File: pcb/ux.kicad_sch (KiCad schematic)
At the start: 41 parts, among them J5 Conn_01x40, J7 GameBoy_LinkPort, J8 Conn_01x02, SW12 A, SW13 B, SW14 START, SW15 SELECT, SW2 BOOT, SW3 RESET, SW4 UP, SW5 DOWN, SW6 LEFT, SW7 RIGHT, U5 APA2502, U7 ICM-42670-P, U8 TCA9535RTWR

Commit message: pcb: Update schematic to WIP6
Change-Id: I9e9f727ad2774ee986f2f97450dc509901129aec
Reviewed-on: https://pigweed-review.googlesource.com/c/pigweed/kudzu/+/169650
Reviewed-by: Anthony DiGirolamo <tonymd@google.com>
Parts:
- added C16 (x2): 10nF, symbol Device:C_Small
- added C17 (x2), C18: 100nF, symbol Device:C_Small
- added C18: 10uF, symbol Device:C_Small
- added R11 (x5): 10K, symbol Device:R_Small
- added R11: 634K, symbol Device:R_Small
- added R13 (x2): 100K, symbol Device:R_Small
- added RN1, RN2: 10K, Resistor_THT:R_Array_SIP5, symbol Device:R_Pack04
- added TP10 (x5): RUN, symbol Connector:TestPoint
- added U9: MAX98357, symbol kudzu-parts:MAX98357
- D5: Price @ 10 (none) -> 0.07800; Price @ 25 (none) -> 0.07220
- J5: Price @ 10 (none) -> 0.17; Price @ 25 (none) -> 0.17
- J7: Price @ 10 (none) -> 2.09; Price @ 25 (none) -> 2.09
- U5: value APA2502 -> AP2502; DigiKey PN (none) -> AP2502KTR-G1DITR-ND; Price @ 10 (none) -> 0.34400; Price @ 25 (none) -> 0.32080
- U7: DigiKey PN (none) -> 1428-ICM-42670-PCT-ND; Price @ 10 (none) -> 3.66400; Price @ 25 (none) -> 3.25680
- U8: DigiKey PN (none) -> 296-25156-2-ND; Price @ 10 (none) -> 1.09300; Price @ 25 (none) -> 1.03800
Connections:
- net +3V3: now also C18.1, C18.1, R11.1, R11.1, R11.1, R11.1, R11.1, R13.2, RN1.5 (R4.2), RN1.6 (R3.2), RN1.7 (R2.2), RN1.8 (R1.2), RN2.5 (R4.2), RN2.6 (R3.2), RN2.7 (R2.2), RN2.8 (R1.2), U9.7 (VDD), U9.8 (VDD)
- net BUTTON_A: now also U8.5 (P04), RN1.4 (R4.1)
- net BUTTON_B: now also U8.6 (P05), RN1.3 (R3.1)
- net BUTTON_DOWN: now also U8.2 (P01), RN2.3 (R3.1)
- net BUTTON_LEFT: now also U8.3 (P02), RN2.2 (R2.1)
- net BUTTON_RIGHT: now also U8.4 (P03), RN2.1 (R1.1)
- net BUTTON_SELECT: now also U8.7 (P06), RN1.2 (R2.1)
- net BUTTON_START: now also U8.8 (P07), RN1.1 (R1.1)
- net BUTTON_UP: now also U8.1 (P00), RN2.4 (R4.1)
- net CHARGE_STAT: now also U8.17 (P17)
- net DISP_IOVCC: now also C16.2, C17.2
- net DISP_RESET: now also U8.15 (P15)
- net DISP_VCI: now also C16.2, C17.2
- net GND: now also C16.1, C16.1, C17.1, C17.1, C18.2, C18.2, R11.2, R13.1, U9.11 (GND), U9.15 (GND), U9.3 (GND), U9.EP; no longer U7.7 (FSYNC)
- net TOUCH_IRQ: now also R11.2
- net TOUCH_RESET: now also U8.14 (P14), R11.2
- net IMU_INT1: now reaches U7.4 (INT1/INT)
- net IMU_INT1: now also R11.2, TP10.1
- net BOARD_ID0: now reaches U8.10 (P10)
- net BOARD_ID1: now reaches U8.11 (P11)
- net BOARD_ID2: now reaches U8.12 (P12)
- net BOARD_ID3: now reaches U8.13 (P13)
- net GAUGE_QSTRT: now reaches U8.16 (P16)
- net at J8.1 (Pin_1): now also U9.9 (OUTP)
- net at J8.2 (Pin_2): now also U9.10 (OUTN)
- net IMU_INT renamed IMU_INT2
- net IMU_INT2: now also R11.2, TP10.1
- new net AUDIO_BCLK: TP10.1, U9.16 (BCLK)
- new net AUDIO_DATA: TP10.1, U9.1 (DIN)
- new net AUDIO_LRCLK: TP10.1, U9.14 (LRCLK)
- new net AUDIO_SD: R11.2, U9.4 (SD_MODE)
- new net GAIN_SLOT: R13.1, R13.2, U9.2 (GAIN_SLOT)
- new net IMU_FSYNC: R11.1, U7.7 (FSYNC)
- no-connect marks 18 -> 17
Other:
- note added: "0R 210.2K 634K"
- note added: "100K to GND 0R to GND unconnected 0R to +3V3 100K to +3V3"
- note added: "15 12 9 6 3"
- note added: "Audio Channel"
- note added: "GAIN_SLOT connection"
- note added: "Gain (dB)"
- note added: "Left Right L/2 + R/2"
- note added: "SD_MODE Pullup"
- note added: "TODO: Tune current limiting resistors based on actual components"
- note removed: "Board ID"
- moved on the sheet: C16, C17, C18, D1, D3, D5, J7, J8, JP1, JP2, JP4, R10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

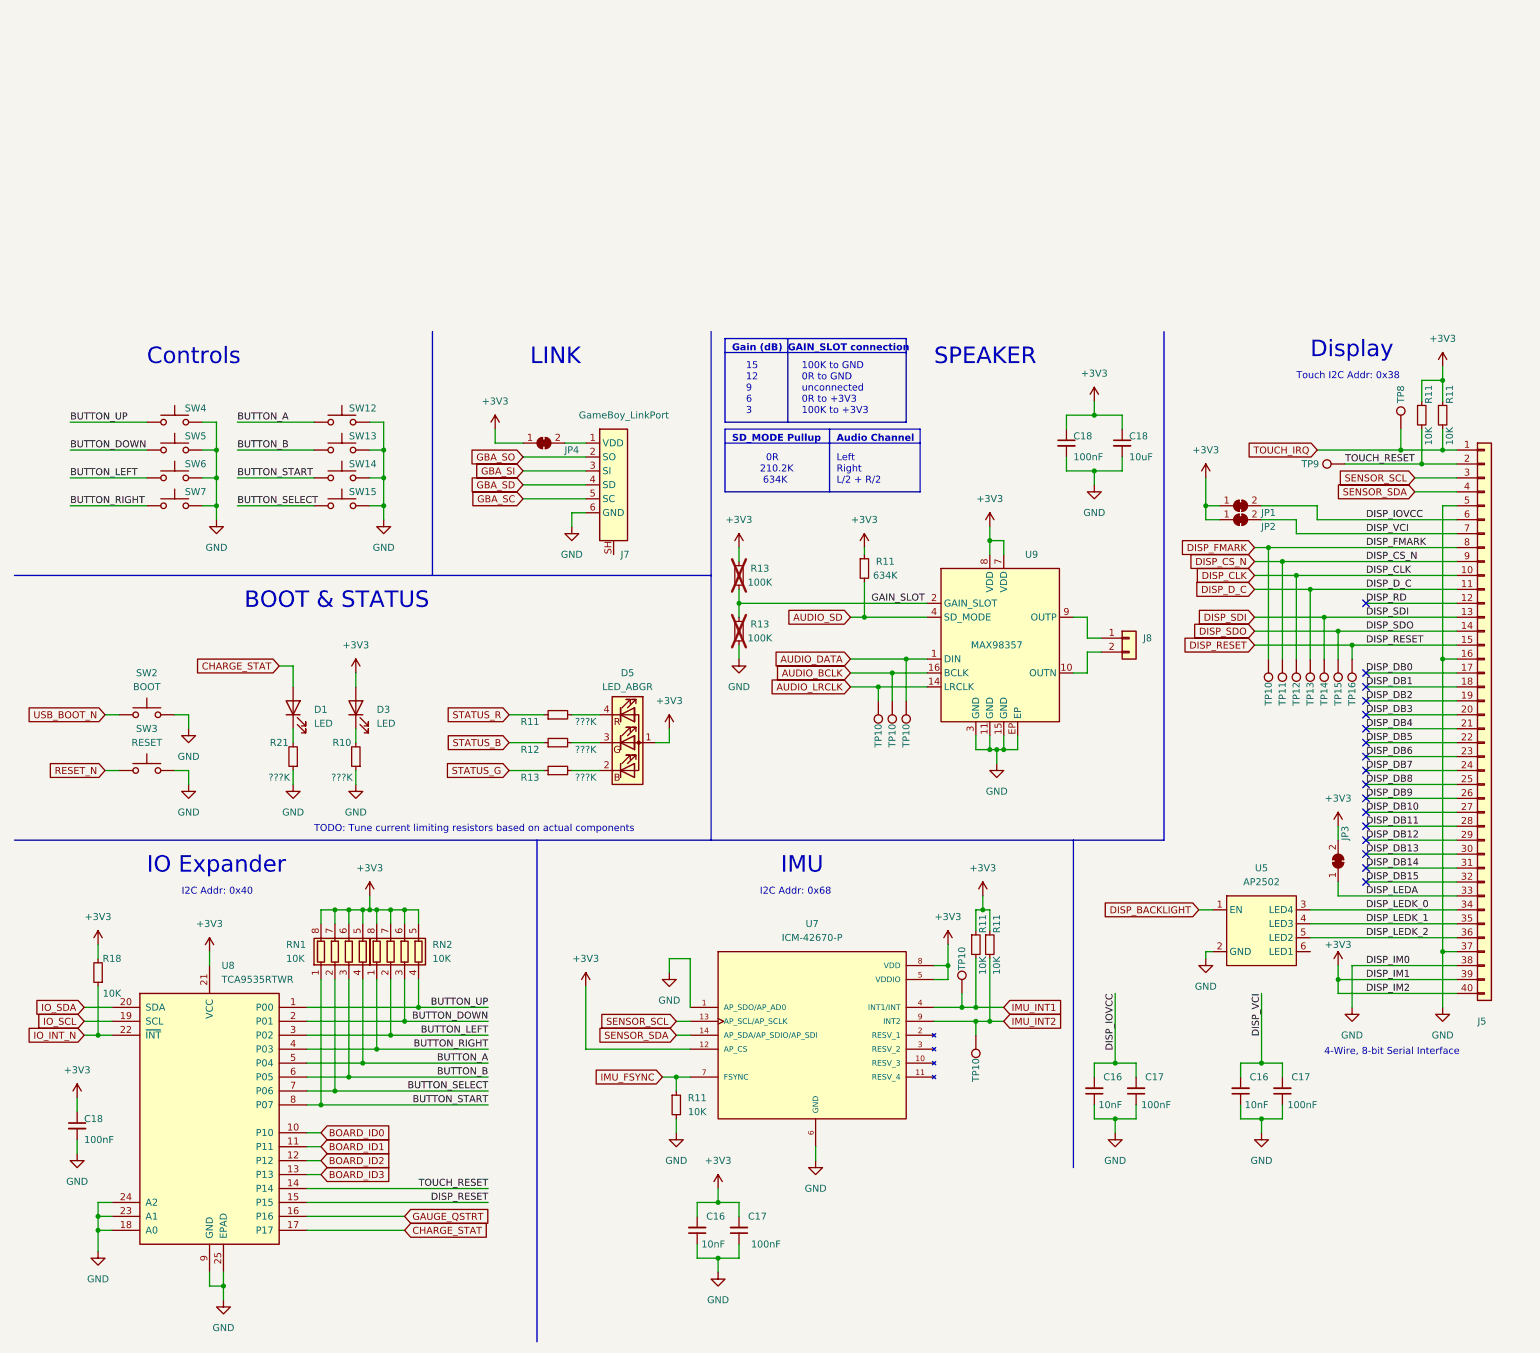
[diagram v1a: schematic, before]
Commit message: pcb: Update pcb to WIP7
Changes:

- Pruned unused parts from `kudzu-parts.kicad_sym`.
- Updated all parts in `kudzu-parts.kicad_sym` to pass `klc-check/check_symbol.py`.
- Switched to `PI4IOE5V6416` IO expander which has programmable pull-up.
- Removed pull-ups on `BOARD_ID*`, `BUTTON_*`, `TOUCH_RESET`, and `DISP_RESET`
  in favor of internal pull-ups in the IO expander.
- Added pull-up to `RESET_N`.
- Removed test points from `QSPI_*`.
- Switched to QFN version of `MCP73831`.
- Fixed missing pin number on `MAX17048` `QSTRT`.
- Removed pull-up on 3.3V regulator's `EN` pin and tied directly to `VIN`.
- Added extra decoupling caps to rp2040's 3.3V and 1.1V lines per design guide.
- Added note to add axis diagram to silk screen on board.
- Miscellaneous visual cleanup.
- Added FET on conduction path for system power.
- Added circuit to charge at 250mA when system is on and 500mA when system is off.
- Assigned all RP2040 IOs.
- Created and switched to dedicated symbols for DPAD, A/B, and SELECT/START.
- Switched display connector symbol for one with a mounting pin.
- Set test point values to net names.
- Selected LEDs and current limiting resistor values.
- Added closed solder jumpers to GBA Link signals.
- Changed solder jumper on GBA VCC pin to open.
- Changed LCD decoupling to mach reference circuit.
- Connected DISP_RD (J9 Pin 12) to +3V3.
- Connected DB0-15 (J9 Pins 17-32) to GND.
- Updated 12MHz Crystal (Y1) to correct symbol and foot print.

Change-Id: I6d0fe442c50df116031305f5165b6a29d3572d45
Reviewed-on: https://pigweed-review.googlesource.com/c/pigweed/kudzu/+/169858
Reviewed-by: Anthony DiGirolamo <tonymd@google.com>
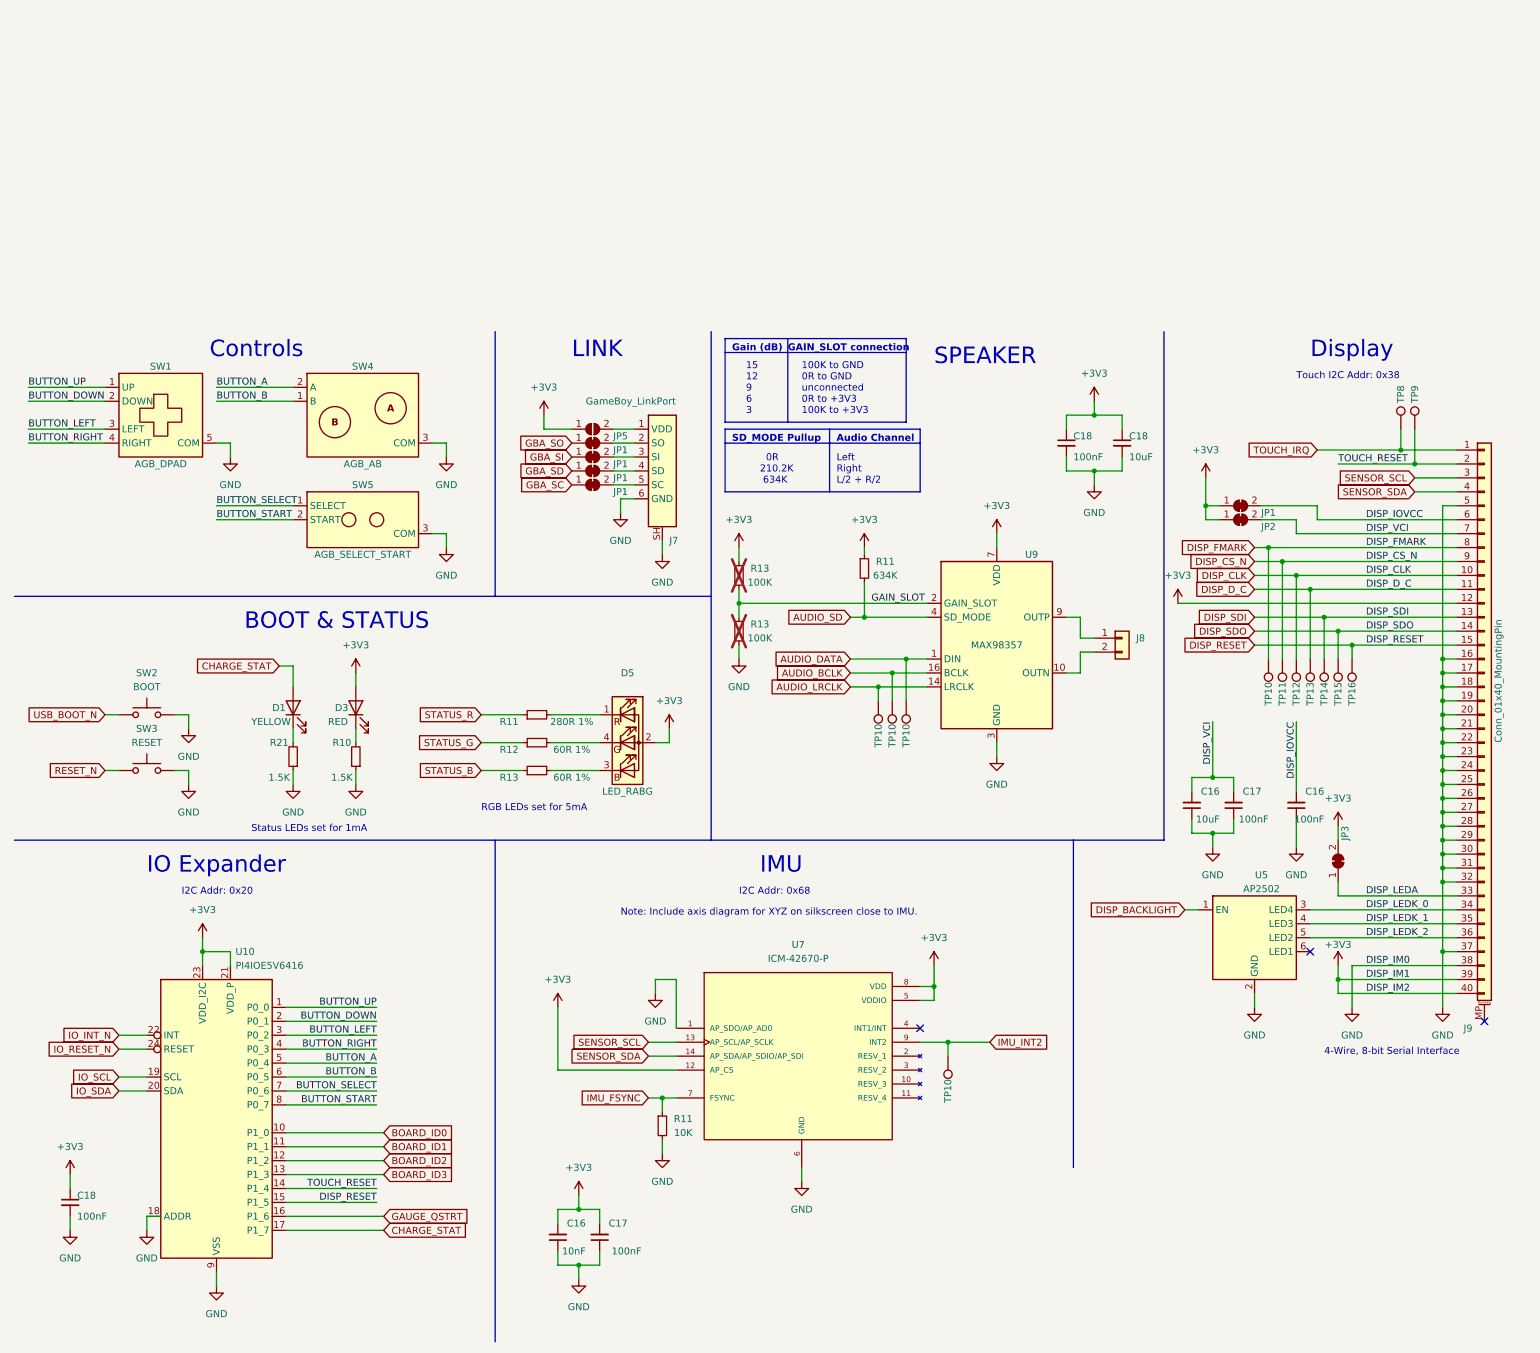
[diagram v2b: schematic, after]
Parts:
- removed C17: 100nF, symbol Device:C_Small
- removed J5: Conn_01x40, symbol Connector_Generic:Conn_01x40
- removed JP4: SolderJumper_2_Bridged, symbol Jumper:SolderJumper_2_Bridged
- removed R11 (x4), R18: 10K, symbol Device:R_Small
- removed RN1, RN2: 10K, Resistor_THT:R_Array_SIP5, symbol Device:R_Pack04
- removed SW12: A, symbol Switch:SW_Push
- removed SW13: B, symbol Switch:SW_Push
- removed SW14: START, symbol Switch:SW_Push
- removed SW15: SELECT, symbol Switch:SW_Push
- removed SW4: UP, symbol Switch:SW_Push
- removed SW5: DOWN, symbol Switch:SW_Push
- removed SW6: LEFT, symbol Switch:SW_Push
- removed SW7: RIGHT, symbol Switch:SW_Push
- removed TP10: RUN, symbol Connector:TestPoint
- removed U8: TCA9535RTWR, Package_DFN_QFN:WQFN-24-1EP_4x4mm_P0.5mm_EP2.45x2.45mm, symbol Interface_Expansion:TCA9535RTWR
- added J9: Conn_01x40_MountingPin, KudzuLibrary:FPC-Connector_1x40-1MP_P0.50mm_Horizontal, symbol Connector_Generic_MountingPin:Conn_01x40_MountingPin
- added JP1: GBA_SD, Jumper:SolderJumper-2_P1.3mm_Bridged_RoundedPad1.0x1.5mm, symbol Jumper:SolderJumper_2_Bridged
- added JP1: GBA_SC, Jumper:SolderJumper-2_P1.3mm_Bridged_RoundedPad1.0x1.5mm, symbol Jumper:SolderJumper_2_Bridged
- added JP1: GBA_SI, Jumper:SolderJumper-2_P1.3mm_Bridged_RoundedPad1.0x1.5mm, symbol Jumper:SolderJumper_2_Bridged
- added JP1: GBA_SO, Jumper:SolderJumper-2_P1.3mm_Bridged_RoundedPad1.0x1.5mm, symbol Jumper:SolderJumper_2_Bridged
- added JP5: GBA_VDD, Jumper:SolderJumper-2_P1.3mm_Open_RoundedPad1.0x1.5mm, symbol Jumper:SolderJumper_2_Open
- added SW1: AGB_DPAD, KudzuLibrary:GBA_DPad, symbol kudzu-parts:AGB_DPAD
- added SW4: AGB_AB, KudzuLibrary:GBA_AB, symbol kudzu-parts:AGB_AB
- added SW5: AGB_SELECT_START, KudzuLibrary:GBA_StartSelect, symbol kudzu-parts:AGB_SELECT_START
- added U10: PI4IOE5V6416, Package_DFN_QFN:TQFN-24-1EP_4x4mm_P0.5mm_EP2.1x2.1mm_ThermalVias, symbol kudzu-parts:PI4IOE5V6416
- C16: value 10nF -> 100nF; footprint (none) -> Capacitor_SMD:C_0603_1608Metric
- C16, C17, C18: footprint (none) -> Capacitor_SMD:C_0603_1608Metric
- C16: value 10nF -> 10uF; footprint (none) -> Capacitor_SMD:C_0603_1608Metric
- D1: value LED -> YELLOW; footprint (none) -> LED_SMD:LED_0603_1608Metric; Forward Voltage (none) -> 1.8
- D3: value LED -> RED; footprint (none) -> LED_SMD:LED_0603_1608Metric; Forward Voltage (none) -> 1.8
- D5: value LED_ABGR -> LED_RABG; footprint (none) -> LED_SMD:LED_Cree-PLCC4_3.2x2.8mm_CCW; symbol Device:LED_ABGR -> Device:LED_RABG; DigiKey PN UHD1110-FKA-CL1A13R3Q1BBQFMF3CT-ND -> 1830-1116-1-ND; Price @ 10 0.07800 -> 0.30300; Price @ 25 0.07220 -> 0.17420
- J7: footprint (none) -> Gekkio_Connector:GameBoy_LinkPort_MGB_Horizontal
- J8: footprint (none) -> Connector_Molex:Molex_PicoBlade_53048-0210_1x02_P1.25mm_Horizontal
- JP1, JP2, JP3: footprint (none) -> Jumper:SolderJumper-2_P1.3mm_Bridged_RoundedPad1.0x1.5mm
- R10, R21: value ???K -> 1.5K; footprint (none) -> Resistor_SMD:R_0603_1608Metric
- R11: value ???K -> 280R 1%; footprint (none) -> Resistor_SMD:R_0603_1608Metric
- R11, R13: footprint (none) -> Resistor_SMD:R_0603_1608Metric
- R12, R13: value ???K -> 60R 1%; footprint (none) -> Resistor_SMD:R_0603_1608Metric
- SW2, SW3: footprint (none) -> Button_Switch_SMD:SW_Push_1P1T_NO_CK_KMR2; DigiKey PN (none) -> 401-1427-1-ND; Price @ 10 (none) -> 0.50700; Price @ 25 (none) -> 0.48840
- TP10: value RUN -> AUDIO_BCLK; footprint (none) -> TestPoint:TestPoint_Pad_D1.0mm
- TP10: value RUN -> DISP_FMARK; footprint (none) -> TestPoint:TestPoint_Pad_D1.0mm
- TP10: value RUN -> AUDIO_LRCLK; footprint (none) -> TestPoint:TestPoint_Pad_D1.0mm
- TP10: value RUN -> IMU_INT2; footprint (none) -> TestPoint:TestPoint_Pad_D1.0mm
- TP10: value RUN -> AUDIO_DATA; footprint (none) -> TestPoint:TestPoint_Pad_D1.0mm
- TP11: value RUN -> DISP_CS_N; footprint (none) -> TestPoint:TestPoint_Pad_D1.0mm
- TP12: value RUN -> DISP_CLK; footprint (none) -> TestPoint:TestPoint_Pad_D1.0mm
- TP13: value RUN -> DISP_D_C; footprint (none) -> TestPoint:TestPoint_Pad_D1.0mm
- TP14: value RUN -> DISP_SDI; footprint (none) -> TestPoint:TestPoint_Pad_D1.0mm
- TP15: value RUN -> DISP_SDO; footprint (none) -> TestPoint:TestPoint_Pad_D1.0mm
- TP16: value RUN -> DISP_RESET; footprint (none) -> TestPoint:TestPoint_Pad_D1.0mm
- TP8: value RUN -> TOUCH_IRQ; footprint (none) -> TestPoint:TestPoint_Pad_D1.0mm
- TP9: value RUN -> TOUCH_RESET; footprint (none) -> TestPoint:TestPoint_Pad_D1.0mm
- U5: footprint (none) -> Package_TO_SOT_SMD:SOT-23-6
- U7: footprint IC_ICM-42670-P -> Rust_Board:IC_ICM-42670-P
- U9: footprint (none) -> Package_DFN_QFN:TQFN-16-1EP_3x3mm_P0.5mm_EP1.23x1.23mm_ThermalVias
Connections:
- net +3V3: now also D5.2 (A), J9.12 (Pin_12), J9.39 (Pin_39), J9.40 (Pin_40), JP5.1 (A), U10.21 (VDD_P), U10.23 (VDD_I2C); no longer D5.1 (A)
- net BOARD_ID0: now also U10.10 (P1_0)
- net BOARD_ID1: now also U10.11 (P1_1)
- net BOARD_ID2: now also U10.12 (P1_2)
- net BOARD_ID3: now also U10.13 (P1_3)
- net BUTTON_A: now also SW4.2 (A), U10.5 (P0_4)
- net BUTTON_B: now also SW4.1 (B), U10.6 (P0_5)
- net BUTTON_DOWN: now also SW1.2 (DOWN), U10.2 (P0_1)
- net BUTTON_LEFT: now also SW1.3 (LEFT), U10.3 (P0_2)
- net BUTTON_RIGHT: now also SW1.4 (RIGHT), U10.4 (P0_3)
- net BUTTON_SELECT: now also SW5.1 (SELECT), U10.7 (P0_6)
- net BUTTON_START: now also SW5.2 (START), U10.8 (P0_7)
- net BUTTON_UP: now also SW1.1 (UP), U10.1 (P0_0)
- net CHARGE_STAT: now also U10.17 (P1_7)
- net DISP_CLK: now also J9.10 (Pin_10)
- net DISP_CS_N: now also J9.9 (Pin_9)
- net DISP_D_C: now also J9.11 (Pin_11)
- net DISP_FMARK: now also J9.8 (Pin_8)
- net DISP_IOVCC: now also C16.2, J9.6 (Pin_6); no longer C16.2, C17.2
- net DISP_LEDA: now also J9.33 (Pin_33)
- net DISP_LEDK_0: now also J9.34 (Pin_34)
- net DISP_LEDK_1: now also J9.35 (Pin_35)
- net DISP_LEDK_2: now also J9.36 (Pin_36)
- net DISP_RESET: now also J9.15 (Pin_15), U10.15 (P1_5)
- net DISP_SDI: now also J9.13 (Pin_13)
- net DISP_SDO: now also J9.14 (Pin_14)
- net DISP_VCI: now also C16.2, C17.2, J9.7 (Pin_7); no longer C16.2
- net GAUGE_QSTRT: now also U10.16 (P1_6)
- net GBA_SC: now also JP1.1 (A); no longer J7.5 (SC)
- net GBA_SD: now also JP1.1 (A); no longer J7.4 (SD)
- net GBA_SI: now also JP1.1 (A); no longer J7.3 (SI)
- net GBA_SO: now also JP1.1 (A); no longer J7.2 (SO)
- net GND: now also J7.SH, U9.17 (GND), J9.16 (Pin_16), J9.17 (Pin_17), J9.18 (Pin_18), J9.19 (Pin_19), J9.20 (Pin_20), J9.21 (Pin_21), J9.22 (Pin_22), J9.23 (Pin_23), J9.24 (Pin_24), J9.25 (Pin_25), J9.26 (Pin_26), J9.27 (Pin_27), J9.28 (Pin_28), J9.29 (Pin_29), J9.30 (Pin_30), J9.31 (Pin_31), J9.32 (Pin_32), J9.37 (Pin_37), J9.38 (Pin_38), J9.5 (Pin_5), SW1.5 (COM), SW4.3 (COM), SW5.3 (COM), U10.18 (ADDR), U10.25 (VSS), U10.9 (VSS); no longer U9.EP
- net IO_INT_N: now also U10.22 (INT)
- net IO_SCL: now also U10.19 (SCL)
- net IO_SDA: now also U10.20 (SDA)
- net SENSOR_SCL: now also J9.3 (Pin_3)
- net SENSOR_SDA: now also J9.4 (Pin_4)
- net STATUS_B: now also R13.1; no longer R12.1
- net STATUS_G: now also R12.1; no longer R13.1
- net TOUCH_IRQ: now also J9.1 (Pin_1)
- net TOUCH_RESET: now also J9.2 (Pin_2), U10.14 (P1_4)
- net at R12.2: now also D5.4 (GK); no longer D5.3 (GK)
- net at R11.2: now also D5.1 (RK); no longer D5.4 (RK)
- net at R13.2: now also D5.3 (BK); no longer D5.2 (BK)
- net at J7.1 (VDD): now also JP5.2 (B)
- net IMU_INT1: no longer names the net of U7.4 (INT1/INT)
- new net: J7.4 (SD), JP1.2 (B)
- new net: J7.5 (SC), JP1.2 (B)
- new net: J7.3 (SI), JP1.2 (B)
- new net: J7.2 (SO), JP1.2 (B)
- new net IO_RESET_N: U10.24 (RESET)
- no-connect marks 17 -> 3
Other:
- note added: "I2C Addr: 0x20"
- note added: "Note: Include axis diagram for XYZ on silkscreen close to IMU."
- note added: "RGB LEDs set for 5mA"
- note added: "Status LEDs set for 1mA"
- note removed: "I2C Addr: 0x40"
- note removed: "TODO: Tune current limiting resistors based on actual components"
- moved on the sheet: C16, C17, C18, J7, J8, R11, R12, R13, TP10, TP9, U5, U7

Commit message: pcb: rev 0-r1 - board routed
Change-Id: Icb9c0ddbcf21cc7f2bac7bbcd371ff5a97baf35d
Reviewed-on: https://pigweed-review.googlesource.com/c/pigweed/kudzu/+/170233
Reviewed-by: Anthony DiGirolamo <tonymd@google.com>
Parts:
- added C18: 100nF, Capacitor_SMD:C_0603_1608Metric, symbol Device:C_Small
- D1: value YELLOW -> ORANGE; DigiKey PN (none) -> 160-1477-1-ND; Price @ 10 (none) -> 0.12700; Price @ 25 (none) -> 0.12700
- D3: value RED -> GREEN; DigiKey PN (none) -> 160-1475-1-ND; Price @ 10 (none) -> 0.13200; Price @ 25 (none) -> 0.13200
- D5: DigiKey PN 1830-1116-1-ND -> CLVBA-FKA-CA1D181BB7R3R3DKR-ND; Price @ 10 0.30300 -> 0.60000; Price @ 25 0.17420 -> 0.60000
- J8: footprint Connector_Molex:Molex_PicoBlade_53048-0210_1x02_P1.25mm_Horizontal -> KudzuLibrary:CONN HEADER SMD 2POS 1.25MM; DigiKey PN (none) -> WM7620CT-ND; Price @ 10 (none) -> 0.48300; Price @ 25 (none) -> 0.48300
- SW2, SW3: footprint Button_Switch_SMD:SW_Push_1P1T_NO_CK_KMR2 -> KudzuLibrary:SW_Push_1P1T_NO_CK_PTS840_GK_SMTR_LFS; DigiKey PN 401-1427-1-ND -> CKN10508CT-ND; Price @ 10 0.50700 -> 0.43900; Price @ 25 0.48840 -> 0.41360
- U10: footprint Package_DFN_QFN:TQFN-24-1EP_4x4mm_P0.5mm_EP2.1x2.1mm_ThermalVias -> Package_DFN_QFN:TQFN-24-1EP_4x4mm_P0.5mm_EP2.1x2.1mm
- U9: footprint Package_DFN_QFN:TQFN-16-1EP_3x3mm_P0.5mm_EP1.23x1.23mm_ThermalVias -> Package_DFN_QFN:TQFN-16-1EP_3x3mm_P0.5mm_EP1.23x1.23mm
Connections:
- net +3V3: now also C18.1
- net BOARD_ID0: now also U10.11 (P1_1); no longer U10.10 (P1_0)
- net BOARD_ID1: now also U10.12 (P1_2); no longer U10.11 (P1_1)
- net BOARD_ID2: now also U10.13 (P1_3); no longer U10.12 (P1_2)
- net BOARD_ID3: now also U10.14 (P1_4); no longer U10.13 (P1_3)
- net BUTTON_A: now also U10.8 (P0_7); no longer U10.5 (P0_4)
- net BUTTON_B: now also U10.7 (P0_6); no longer U10.6 (P0_5)
- net BUTTON_DOWN: now also U10.4 (P0_3); no longer U10.2 (P0_1)
- net BUTTON_RIGHT: now also U10.2 (P0_1); no longer U10.4 (P0_3)
- net BUTTON_SELECT: now also U10.5 (P0_4); no longer U10.7 (P0_6)
- net BUTTON_START: now also U10.6 (P0_5); no longer U10.8 (P0_7)
- net CHARGE_STAT: now also U10.10 (P1_0); no longer U10.17 (P1_7)
- net DISP_LEDK_0: now also U5.6 (LED1); no longer U5.3 (LED4)
- net DISP_LEDK_1: now also U5.5 (LED2); no longer U5.4 (LED3)
- net DISP_LEDK_2: now also U5.4 (LED3); no longer U5.5 (LED2)
- net DISP_RESET: now also U10.16 (P1_6); no longer U10.15 (P1_5)
- net GAUGE_QSTRT: now also U10.15 (P1_5); no longer U10.16 (P1_6)
- net GND: now also C18.2
- net TOUCH_RESET: now also U10.17 (P1_7); no longer U10.14 (P1_4)
- net at J8.1 (Pin_1): now also U9.10 (OUTN); no longer U9.9 (OUTP)
- net at J8.2 (Pin_2): now also U9.9 (OUTP); no longer U9.10 (OUTN)
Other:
- company: (none) -> Copyright 2023 The Pigweed Authors
- moved on the sheet: U5
